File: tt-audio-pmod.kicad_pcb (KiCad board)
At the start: 2 copper layers, 45.7 x 20.3 mm, 18 parts, among them J1 10129382-912001BLF, J2 Female header, J4 Male header, J5 PJ-320B, U1 74LVCE1G126SE-7

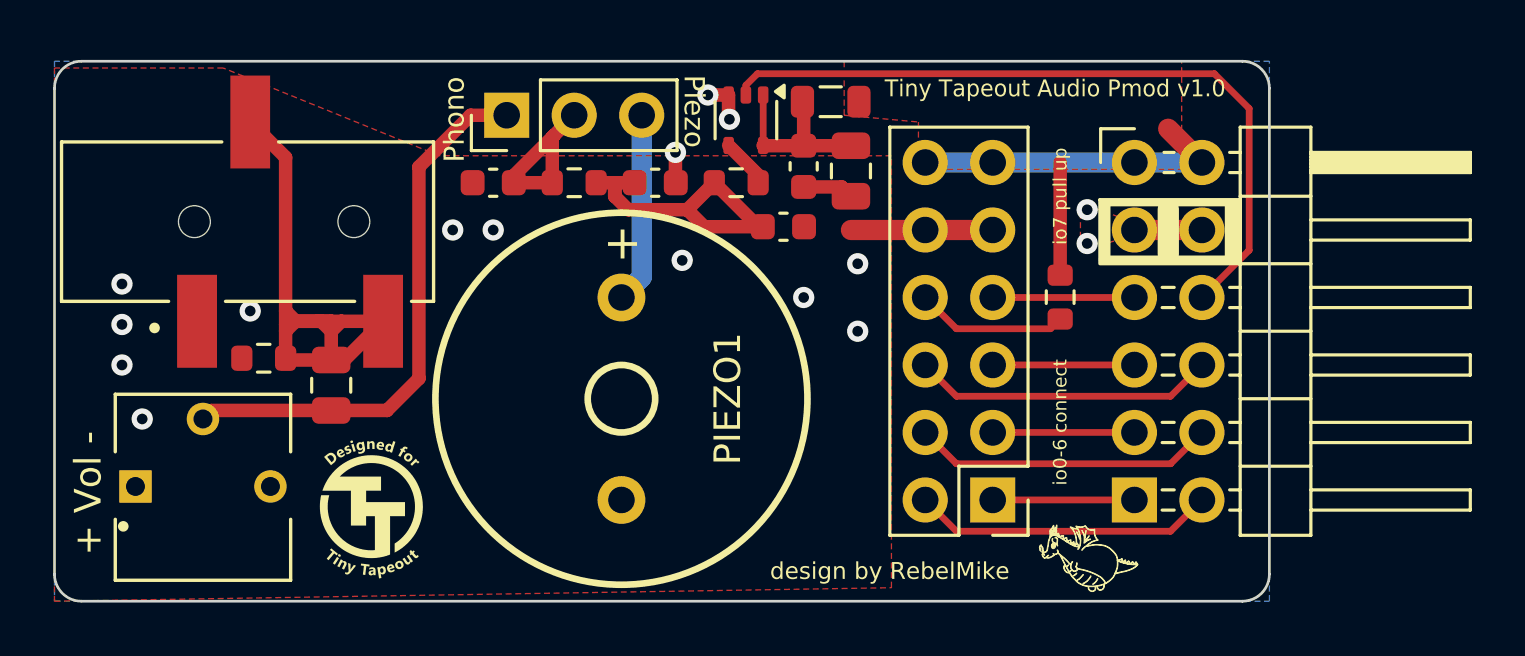
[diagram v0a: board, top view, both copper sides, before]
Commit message: Silkscreen and BOM updates
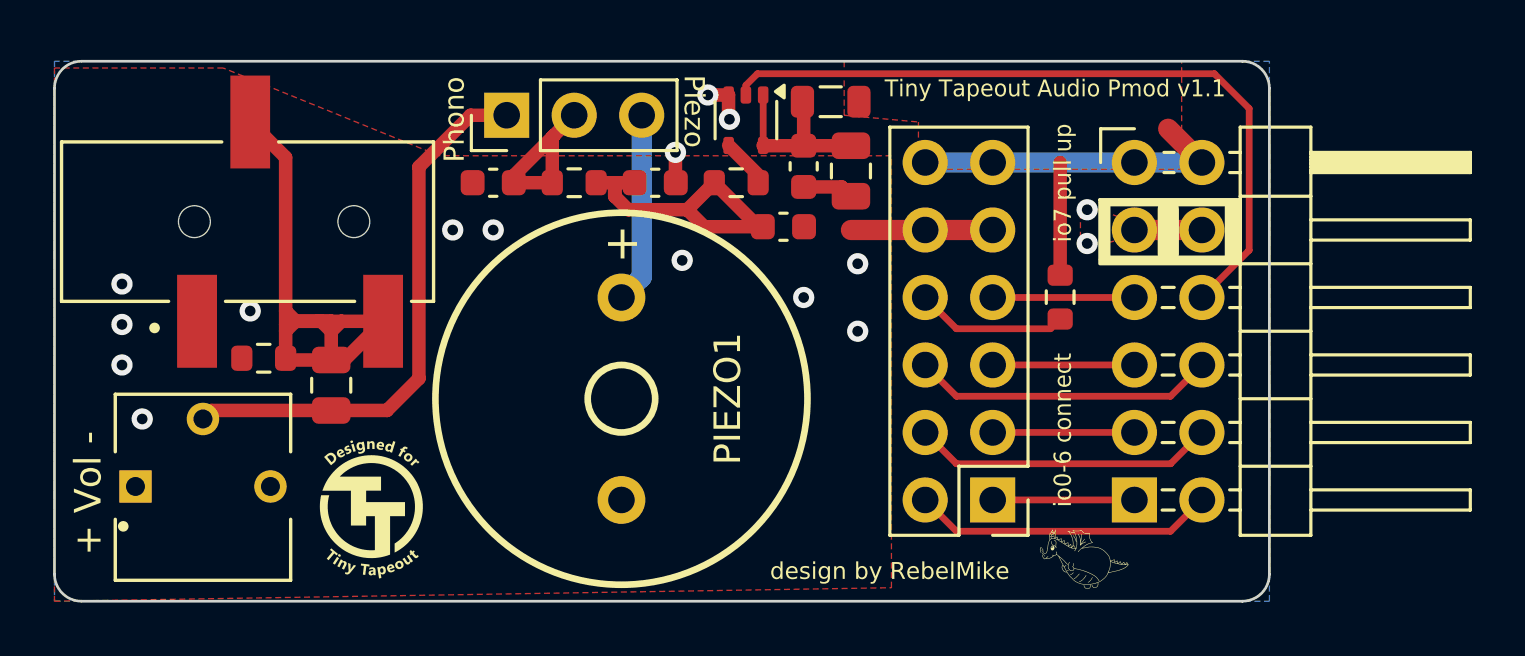
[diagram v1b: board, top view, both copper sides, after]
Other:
- board text added: "Tiny Tapeout Audio Pmod v1.1"
- board text removed: "Tiny Tapeout Audio Pmod v1.0"
